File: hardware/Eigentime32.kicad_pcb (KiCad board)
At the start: 2 copper layers, 40 x 40 mm, 0 parts

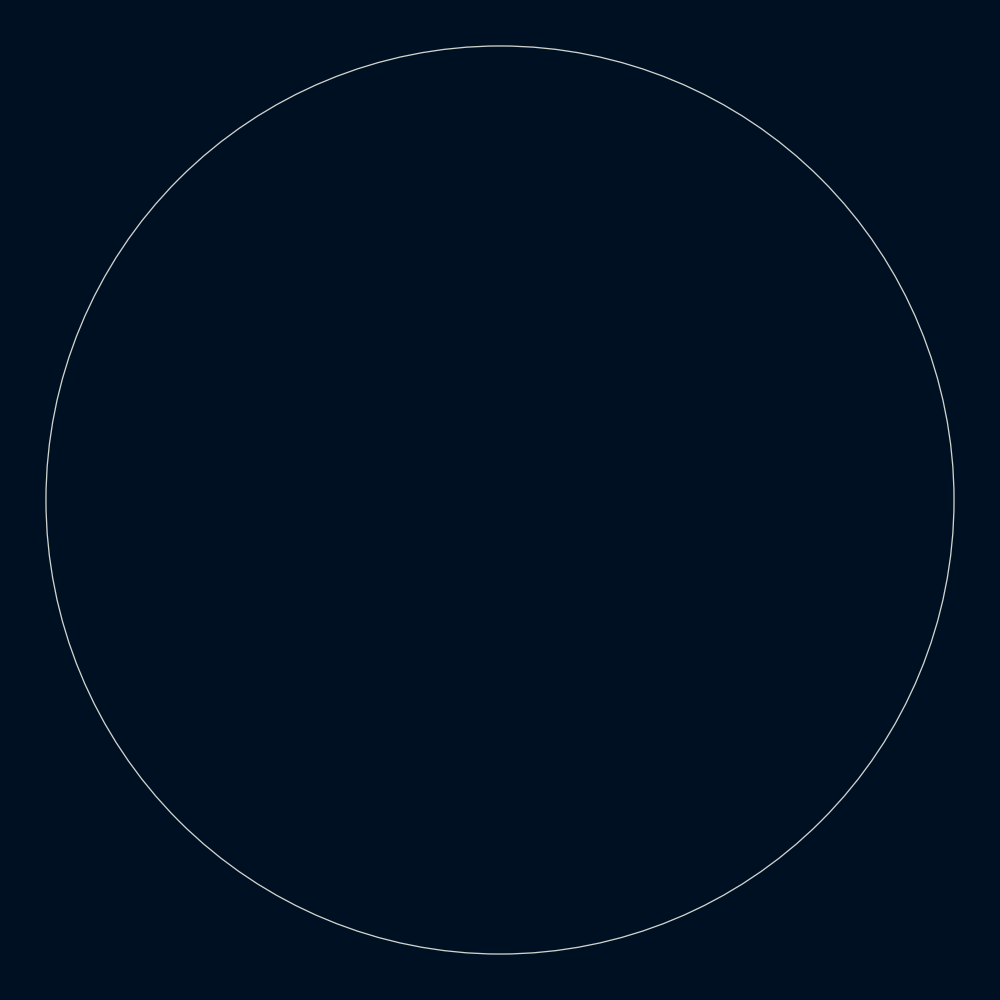
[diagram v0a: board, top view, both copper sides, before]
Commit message: 4-layer routed board with the LCD folded under the glass (#3)
* Layout phase 1: placement, NFC coil, part picks for TBD footprints

Board: 40 mm round, 0.8 mm, 2 layers. Front carries only the NFC coil
(LCD keep-out rule area); every other part is on the back around the
centred CR2032 holder (nothing taller than its 4.06 mm). Buttons at
12 o'clock, hinge mark at 9, lid sensor at 3, LCD FPC connector at 6.
Rules: 0.15 mm clearance, 0.2 mm tracks, 0.5/0.3 mm vias, 0.3 mm
copper-to-edge. A rule area forbids copper pour anywhere inside the
coil. Reference designators are on the fab layers.

NFC coil: 8-turn Archimedean spiral on F.Cu, 38.1 mm OD, 0.15/0.15 mm,
built as one polygon in a net-tie footprint (AE1) with plated terminal
vias at 4-5 o'clock next to U8.

Parts: lid sensor is now an Allegro CT8132SK-IS3 TMR switch (push-pull,
no pull-up; SMD NC reeds don't fit and the Coto RR122 is obsolete);
buttons are Panasonic EVQ-P7A01P side-push switches. MCU sheet, BOM
and docs updated. KiCad-written project defaults in .kicad_pro are
included.

ERC clean; DRC: 0 violations, 0 parity issues, only unrouted nets.
Renders in docs/renders.

Co-Authored-By: Claude Opus 5.5 (1M context) <noreply@anthropic.com>

* Layout: re-place parts around the CR2032 insertion channel

The Keystone 3034 is a tunnel retainer: the cell slides in flat from
12 o'clock with ~0.5 mm headroom, so a 21 mm wide path from the holder
to the board edge must be free of parts. A back-side rule area now
keeps it clear. The MCU, RTC and buttons moved out of it: MCU and RTC
on the right, buttons at ~10 and ~2 o'clock, lid sensor at ~4, SWD
pads at ~7:30, power on the left.

The TC2030 footprint is a project copy whose small via keep-out allows
nearby footprints (KiCad checks footprint keep-outs against bounding
boxes, and the holder's box covered it).

DRC: 0 violations, 0 parity issues; nets still unrouted.

Co-Authored-By: Claude Opus 5.5 (1M context) <noreply@anthropic.com>

* Layout: MCU to 4:30, smaller 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
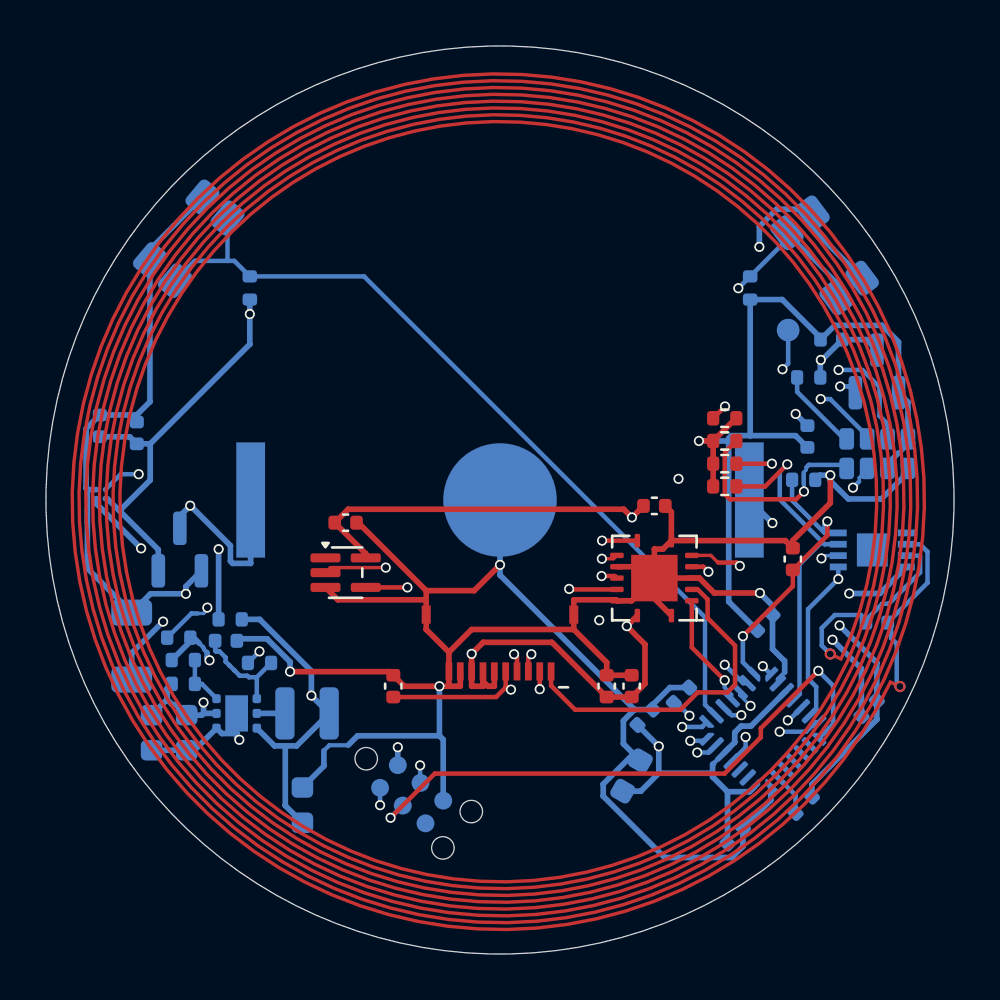
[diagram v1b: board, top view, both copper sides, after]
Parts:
- added AE1: NFC coil, Eigentime32:NFC_PCB_Coil_D38.1mm_8T, F.Cu at (148.5, 105.0)
- added BT1: CR2032, Eigentime32:BatteryHolder_Keystone_3034_1x20mm_SmallNegPad, B.Cu at (148.5, 105.0)
- added C10: 100n, Capacitor_SMD:C_0402_1005Metric, B.Cu at (154.9, 114.6)
- added C11: 100n, Capacitor_SMD:C_0402_1005Metric, B.Cu at (164.8, 114.2)
- added C12: 100n, Capacitor_SMD:C_0402_1005Metric, B.Cu at (160.2, 110.4)
- added C13: 1u, Capacitor_SMD:C_0402_1005Metric, B.Cu at (158.9, 119.8)
- added C14: 10u, Capacitor_SMD:C_0603_1608Metric, B.Cu at (154.3, 117.2)
- added C15: 100n, Capacitor_SMD:C_0402_1005Metric, B.Cu at (156.5, 113.6)
- added C16: 100n, Capacitor_SMD:C_0402_1005Metric, F.Cu at (155.3, 105.3)
- added C17: 100n, Capacitor_SMD:C_0402_1005Metric, F.Cu at (141.7, 106.0)
- added C18: 1u, Capacitor_SMD:C_0402_1005Metric, F.Cu at (153.2, 113.2)
- added C19: 1u, Capacitor_SMD:C_0402_1005Metric, F.Cu at (154.3, 113.2)
- added C2: 100u, Capacitor_SMD:C_1206_3216Metric, B.Cu at (132.3, 111.4)
- added C20: 100n, Capacitor_SMD:C_0402_1005Metric, F.Cu at (143.8, 113.2)
- added C21: 100n, Capacitor_SMD:C_0402_1005Metric, F.Cu at (161.4, 107.6)
- added C22: DNP, Capacitor_SMD:C_0402_1005Metric, B.Cu at (165.1, 110.4)
- added C23: 1u, Capacitor_SMD:C_0402_1005Metric, B.Cu at (163.1, 97.9)
- added C3: 100n, Capacitor_SMD:C_0402_1005Metric, B.Cu at (132.5, 102.0)
- added C4: 10u, Capacitor_SMD:C_0603_1608Metric, B.Cu at (139.8, 118.4)
- added C5: 10u, Capacitor_SMD:C_0603_1608Metric, B.Cu at (134.7, 115.2)
- added C6: 10u, Capacitor_SMD:C_0603_1608Metric, B.Cu at (133.2, 115.2)
- added C7: 1u, Capacitor_SMD:C_0402_1005Metric, B.Cu at (130.9, 101.7)
- added C8: 470n, Capacitor_SMD:C_0402_1005Metric, B.Cu at (136.4, 111.2)
- added C9: 100n, Capacitor_SMD:C_0402_1005Metric, B.Cu at (162.0, 102.2)
- added J1: TC2030-NL, Eigentime32:Tag-Connect_TC2030-IDC-NL_2x03_P1.27mm_Vertical_FootprintsAllowed, B.Cu at (144.6, 118.0)
- added J2: AYF531035, Eigentime32:Panasonic_AYF531035_1x10-1MP_P0.5mm_Horizontal, F.Cu at (148.5, 112.5)
- added L1: 1u, Inductor_SMD:L_Wuerth_MAPI-2512, B.Cu at (140.0, 114.4)
- added Q1: DMG2305UX, Package_TO_SOT_SMD:SOT-23, B.Cu at (134.4, 107.2)
- added R1: 402k, Resistor_SMD:R_0402_1005Metric, B.Cu at (134.6, 113.1)
- added R10: 10k, Resistor_SMD:R_0402_1005Metric, B.Cu at (161.9, 118.4)
- added R12: 1M, Resistor_SMD:R_0402_1005Metric, B.Cu at (137.5, 95.7)
- added R13: 1M, Resistor_SMD:R_0402_1005Metric, B.Cu at (159.5, 95.7)
- added R14: 1M, Resistor_SMD:R_0402_1005Metric, F.Cu at (158.4, 104.4)
- added R15: 100k, Resistor_SMD:R_0402_1005Metric, B.Cu at (161.9, 104.1)
- added R2: 200k, Resistor_SMD:R_0402_1005Metric, B.Cu at (134.6, 112.0)
- added R3: 1M, Resistor_SMD:R_0402_1005Metric, B.Cu at (134.3, 111.1)
- added R4: 470, Resistor_SMD:R_0402_1005Metric, B.Cu at (136.6, 110.3)
- added R5: 1M, Resistor_SMD:R_0402_1005Metric, B.Cu at (137.9, 112.2)
- added R6: 10k, Resistor_SMD:R_0402_1005Metric, F.Cu at (158.4, 101.4)
- added R7: 10k, Resistor_SMD:R_0402_1005Metric, F.Cu at (158.4, 102.4)
- added R8: 470k, Resistor_SMD:R_0402_1005Metric, F.Cu at (158.4, 103.4)
- added R9: 10k, Resistor_SMD:R_0402_1005Metric, B.Cu at (162.1, 99.6)
- added SW2: BTN1, Button_Switch_SMD:SW_SPST_EVQP7A, B.Cu at (134.8, 93.5)
- added SW3: BTN2, Button_Switch_SMD:SW_SPST_EVQP7A, B.Cu at (162.8, 94.2)
- added TP1: CLKOUT, TestPoint:TestPoint_Pad_D1.0mm, B.Cu at (161.2, 97.5)
- added U1: RV-3032-C7, Package_SON:MicroCrystal_C7_SON-8_1.5x3.2mm_P0.9mm, B.Cu at (165.1, 103.0)
- added U2: STM32L031G6U6, Package_DFN_QFN:QFN-28_4x4mm_P0.5mm, B.Cu at (160.1, 115.1)
- added U3: TPS61099DRV, Package_SON:WSON-6-1EP_2x2mm_P0.65mm_EP1x1.6mm, B.Cu at (136.9, 114.4)
- added U5: TPS22916C, Package_BGA:Texas_PicoStar_BGA-4_0.758x0.758mm_Layout2x2_P0.4mm, B.Cu at (130.9, 104.7)
- added U6: SN74LV4T125, Eigentime32:Texas_RGY0014A_VQFN-14-1EP_3.5x3.5mm_P0.5mm_EP2.05x2.05mm, F.Cu at (155.3, 108.4)
- added U7: SN74LV1T34, Package_TO_SOT_SMD:SOT-353_SC-70-5, F.Cu at (141.7, 108.2)
- added U8: ST25DV04KC-IE6C3, Package_DFN_QFN:DFN-8-1EP_3x2mm_P0.5mm_EP1.36x1.46mm, B.Cu at (164.9, 107.2)
- added U9: CT8132SK-IS3, Package_TO_SOT_SMD:SOT-23, B.Cu at (165.1, 99.3)
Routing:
- net GND: track 0.00 -> 205.7 mm, vias 0 -> 13
- net /VBAT: track 0.00 -> 135.8 mm, vias 0 -> 5
- net /VLCD: track 0.00 -> 55.2 mm, vias 0 -> 4
- net /LCD_PWR_EN: track 0.00 -> 36.7 mm, vias 0 -> 4
- net /MCU/BTN1_N: track 0.00 -> 36.6 mm
- net /Power/VBAT_RAW: track 0.00 -> 35.5 mm, vias 0 -> 2
- net /RTC_CLKOUT: track 0.00 -> 34.4 mm, vias 0 -> 3
- net /RTC_INT: track 0.00 -> 33.2 mm, vias 0 -> 3
- net /SDA: track 0.00 -> 26.2 mm, vias 0 -> 3
- net /MCU/SWCLK: track 0.00 -> 26.0 mm, vias 0 -> 2
- net /MCU/BTN2_N: track 0.00 -> 25.8 mm, vias 0 -> 2
- net /Power/VBST_IN: track 0.00 -> 25.0 mm, vias 0 -> 2
- net /SCL: track 0.00 -> 22.0 mm, vias 0 -> 3
- net /MCU/LID_CLOSED_N: track 0.00 -> 22.0 mm, vias 0 -> 3
- net /MCU/SWDIO: track 0.00 -> 21.6 mm, vias 0 -> 2
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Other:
- copper layers 2 -> 4
- board text added: "BUTTONS"
- board text added: "CR2032 IN (slide from 12 o'clock)"
- board text added: "FPC folds under the glass here, keep clear"
- board text added: "HINGE"
- board text added: "LCD 26.6 x 30.3 (front), FPC ledge at 6 o'clock"
- board text added: "LCD FPC"
- board text added: "LID MAGNET"
- board text added: "UNDER PANEL: 1.2 mm GAP, FRONT PARTS <= 1.0 mm HIGH"
